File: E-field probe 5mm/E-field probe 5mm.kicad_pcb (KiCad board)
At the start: 2 copper layers, 100 x 11 mm, 1 part, among them J1 Conn_Coaxial

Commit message: initial design of all probes
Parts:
- moved J1 33.1 mm to (110.9, 96.3)
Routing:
- net Net-(J1-Pad1): track 94.1 -> 52.8 mm
- net GND: vias 0 -> 40
- added copper zone on B.Cu, net GND
- added copper zone on In2.Cu, net GND
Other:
- board size 100 x 11 mm -> 58.7 x 11 mm
- copper layers 2 -> 4
- net class Default: clearance 0.2 -> 0.1; trace_width 0.25 -> 0.706149
- rule trace_clearance: 0.2 -> 0.1
- board text added: "E-field probe 5mm"
- board text removed: "todo: via fence outline shape"

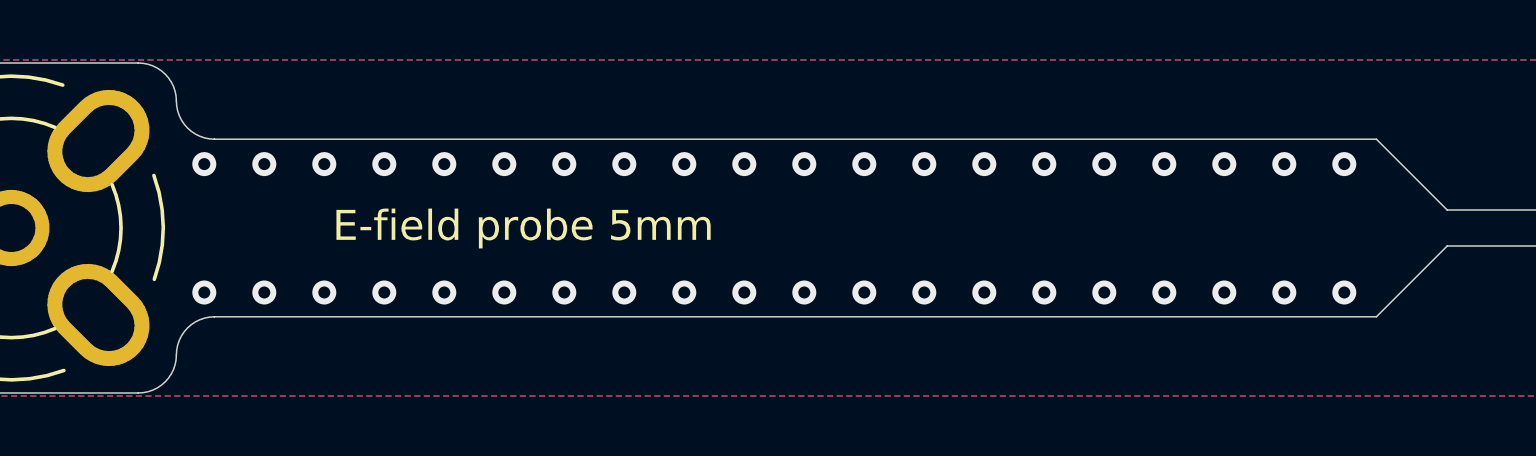
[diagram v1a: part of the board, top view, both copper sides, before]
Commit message: changed via size on handle. Added text and logo
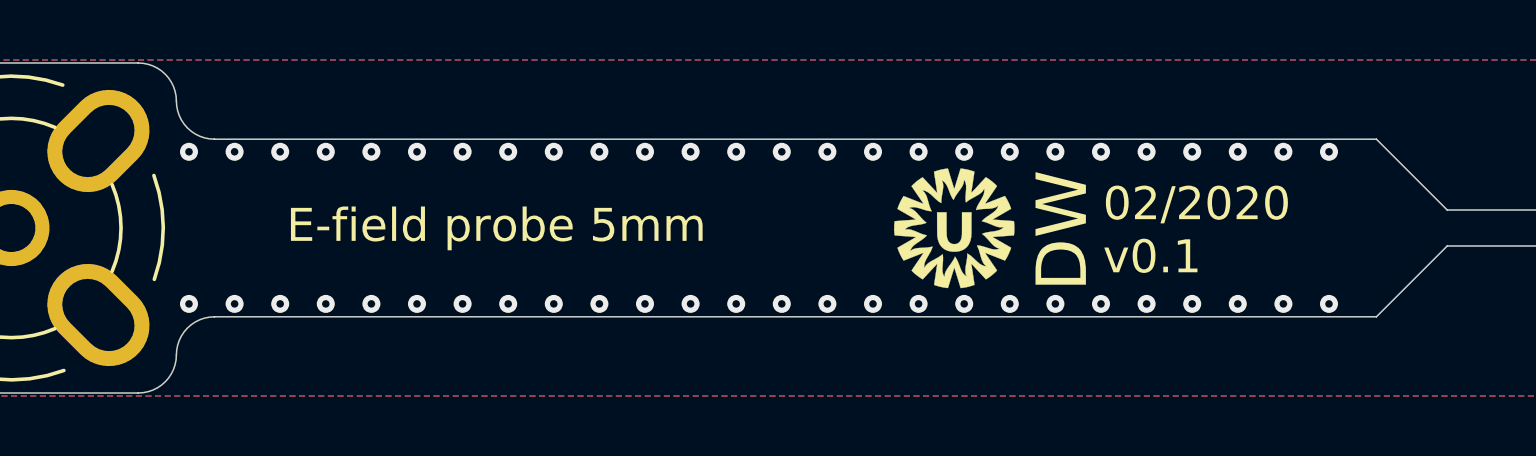
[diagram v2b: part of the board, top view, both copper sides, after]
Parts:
- added G***: LOGO, _Custom:UMC_logo_4mm, F.Cu at (142.3, 96.3)
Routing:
- net GND: vias 40 -> 52
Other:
- board text added: "02/2020 v0.1"
- board text added: "DW"

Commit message: Updated connector
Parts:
- turned J1 to 270 degrees
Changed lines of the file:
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@@
     (add_net "Net-(J1-Pad1)")
+  )
+  (module _Custom:BNC_SMA_Vertical (layer F.Cu)
+    (at 110.88 96.27 270)
+    (descr "BNC female PCB mount 4 pin straight chassis connector http://www.te.com/usa-en/product-1-1478204-0.html")
+    (tags "BNC female PCB mount 4 pin straight chassis connector ")
+    (fp_text reference J1 (at -4.33 0.01) (layer F.SilkS) hide
+      (effects (font (size 1 1) (thickness 0.15)))
+    )
+    (fp_text value Conn_Coaxial (at 0 6.5 90) (layer F.Fab)
+      (effects (font (size 1 1) (thickness 0.15)))
+    )
+    (fp_line (start -2.54 5.08) (end 2.54 5.08) (layer F.SilkS) (width 0.12))
+    (fp_text user %R (at 0 0 90) (layer F.Fab)
+      (effects (font (size 1 1) (thickness 0.15)))
+    )
+    (fp_line (start 5.5 -5.5) (end 5.5 5.5) (layer F.CrtYd) (width 0.05))
+    (fp_line (start 5.5 5.5) (end -5.5 5.5) (layer F.CrtYd) (width 0.05))
+    (fp_line (start -5.5 5.5) (end -5.5 -5.5) (layer F.CrtYd) (width 0.05))
+    (fp_line (start -5.5 -5.5) (end 5.5 -5.5) (layer F.CrtYd) (width 0.05))
+    (fp_circle (center 0 0) (end 4.8 0) (layer F.Fab) (width 0.1))
+    (fp_arc (start 0 0) (end -4.75 1.75) (angle 40) (layer F.SilkS) (width 0.12))
+    (fp_arc (start 0 0) (end 4.75 -1.75) (angle 40) (layer F.SilkS) (width 0.12))
+    (fp_arc (start 0 0) (end -1.75 -4.75) (angle 40) (layer F.SilkS) (width 0.12))
+    (fp_circle (center 0 0) (end 3.175 0) (layer F.Fab) (width 0.1))
+    (fp_arc (start 0 0) (end 3.355 -1.45) (angle 46.74710926) (layer F.SilkS) (width 0.12))
+    (fp_arc (start 0 0) (end -3.355 1.45) (angle 46.74710926) (layer F.SilkS) (width 0.12))
+    (fp_arc (start 0 0) (end -1.45 -3.355) (angle 46.74710926) (layer F.SilkS) (width 0.12))
+    (fp_arc (start 0 0) (end 1.45 3.355) (angle 46.74710926) (layer F.SilkS) (width 0.12))
+    (pad 2 thru_hole oval (at -2.9 -2.9 315) (size 2.7 3.7) (drill oval 1.7 2.7) (layers *.Cu *.Mask)
+      (net 2 GND))
+    (pad 1 thru_hole circle (at 0 0 270) (size 2.54 2.54) (drill 1.6) (layers *.Cu *.Mask)
+      (net 1 "Net-(J1-Pad1)"))
+    (pad 2 thru_hole oval (at 2.9 -2.9 225) (size 2.7 3.7) (drill oval 1.7 2.7) (layers *.Cu *.Mask)
+      (net 2 GND))
+    (pad 2 thru_hole oval (at -2.9 2.9 225) (size 2.7 3.7) (drill oval 1.7 2.7) (layers *.Cu *.Mask)
+      (net 2 GND))
+    (pad 2 thru_hole oval (at 2.9 2.9 315) (size 2.7 3.7) (drill oval 1.7 2.7) (layers *.Cu *.Mask)
+      (net 2 GND))
+    (model :_Custom_3D:BNC_73171-3356.stp
+      (offset (xyz 0 -22.7 6.1))
+      (scale (xyz 1 1 1))
+      (rotate (xyz -90 0 0))
+    )
   )
   (module _Custom:UMC_logo_4mm (layer F.Cu)
@@
       (xy 0.212034 -1.990841)) (layer F.SilkS) (width 0.01))
   )
-  (module _Custom:BNC_SMA_Vertical (layer F.Cu)
-    (at 110.88 96.27)
-    (descr "BNC female PCB mount 4 pin straight chassis connector http://www.te.com/usa-en/product-1-1478204-0.html")
-    (tags "BNC female PCB mount 4 pin straight chassis connector ")
-    (fp_text reference J1 (at -4.33 0.01 90) (layer F.SilkS) hide
-      (effects (font (size 1 1) (thickness 0.15)))
-    )
-    (fp_text value Conn_Coaxial (at 0 6.5) (layer F.Fab)
-      (effects (font (size 1 1) (thickness 0.15)))
-    )
-    (fp_arc (start 0 0) (end 1.45 3.355) (angle 46.74710926) (layer F.SilkS) (width 0.12))
-    (fp_arc (start 0 0) (end -1.45 -3.355) (angle 46.74710926) (layer F.SilkS) (width 0.12))
-    (fp_arc (start 0 0) (end -3.355 1.45) (angle 46.74710926) (layer F.SilkS) (width 0.12))
-    (fp_arc (start 0 0) (end 3.355 -1.45) (angle 46.74710926) (layer F.SilkS) (width 0.12))
-    (fp_circle (center 0 0) (end 3.175 0) (layer F.Fab) (width 0.1))
-    (fp_arc (start 0 0) (end -1.75 -4.75) (angle 40) (layer F.SilkS) (width 0.12))
-    (fp_arc (start 0 0) (end 4.75 -1.75) (angle 40) (layer F.SilkS) (width 0.12))
-    (fp_arc (start 0 0) (end 1.75 4.75) (angle 40) (layer F.SilkS) (width 0.12))
-    (fp_arc (start 0 0) (end -4.75 1.75) (angle 40) (layer F.SilkS) (width 0.12))
-    (fp_circle (center 0 0) (end 4.8 0) (layer F.Fab) (width 0.1))
-    (fp_line (start -5.5 -5.5) (end 5.5 -5.5) (layer F.CrtYd) (width 0.05))
-    (fp_line (start -5.5 5.5) (end -5.5 -5.5) (layer F.CrtYd) (width 0.05))
-    (fp_line (start 5.5 5.5) (end -5.5 5.5) (layer F.CrtYd) (width 0.05))
-    (fp_line (start 5.5 -5.5) (end 5.5 5.5) (layer F.CrtYd) (width 0.05))
-    (fp_text user %R (at 0 0) (layer F.Fab)
-      (effects (font (size 1 1) (thickness 0.15)))
-    )
-    (pad 2 thru_hole oval (at 2.9 2.9 45) (size 2.7 3.7) (drill oval 1.7 2.7) (layers *.Cu *.Mask)
-      (net 2 GND))
-    (pad 2 thru_hole oval (at -2.9 2.9 315) (size 2.7 3.7) (drill oval 1.7 2.7) (layers *.Cu *.Mask)
-      (net 2 GND))
-    (pad 2 thru_hole oval (at 2.9 -2.9 315) (size 2.7 3.7) (drill oval 1.7 2.7) (layers *.Cu *.Mask)
-      (net 2 GND))
-    (pad 1 thru_hole circle (at 0 0) (size 2.54 2.54) (drill 1.6) (layers *.Cu *.Mask)
-      (net 1 "Net-(J1-Pad1)") (clearance 0.2))
-    (pad 2 thru_hole oval (at -2.9 -2.9 45) (size 2.7 3.7) (drill oval 1.7 2.7) (layers *.Cu *.Mask)
-      (net 2 GND))
-    (model ${KISYS3DMOD}/Connector_Coaxial.3dshapes/BNC_TEConnectivity_1478204_Vertical.wrl
-      (at (xyz 0 0 0))
-      (scale (xyz 1 1 1))
-      (rotate (xyz 0 0 0))
-    )
-  )
   (dimension 2.96 (width 0.15) (layer Cmts.User)
     (gr_text "2.960 mm" (at 117.925 94.79 90) (layer Cmts.User)
@@
   (gr_line (start 105.38 100.5) (end 105.38 92.04) (layer Edge.Cuts) (width 0.05))
   (gr_line (start 106.65 90.77) (end 115.110001 90.77) (layer Edge.Cuts) (width 0.05))
+  (segment (start 110.88 96.27) (end 163.63 96.27) (width 0.23495) (layer In1.Cu) (net 1))
   (via (at 116.8 98.8) (size 0.6) (drill 0.25) (layers F.Cu B.Cu) (net 2))
   (via (at 116.8 93.73) (size 0.6) (drill 0.25) (layers F.Cu B.Cu) (net 2))
@@
   (via (at 118.32 93.73) (size 0.6) (drill 0.25) (layers F.Cu B.Cu) (net 2))
   (via (at 154.8 98.8) (size 0.6) (drill 0.25) (layers F.Cu B.Cu) (net 2))
-  (segment (start 110.88 96.27) (end 163.63 96.27) (width 0.23495) (layer In1.Cu) (net 1))
   (zone (net 2) (net_name GND) (layer F.Cu) (hatch edge 0.508)
     (connect_pads (clearance 0))
